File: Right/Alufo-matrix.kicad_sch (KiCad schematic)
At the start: 54 parts, among them K11 PG1350, K12 PG1350, K13 PG1350, K14 PG1350, K15 PG1350, K16 PG1350, K21 PG1350, K22 PG1350, K23 PG1350, K24 PG1350, K25 PG1350, K26 PG1350, K31 PG1350, K32 PG1350, K33 PG1350, K34 PG1350, K35 PG1350, K36 PG1350_1½U, K41 PG1350_1½U, K42 PG1350/SKQUCAA010

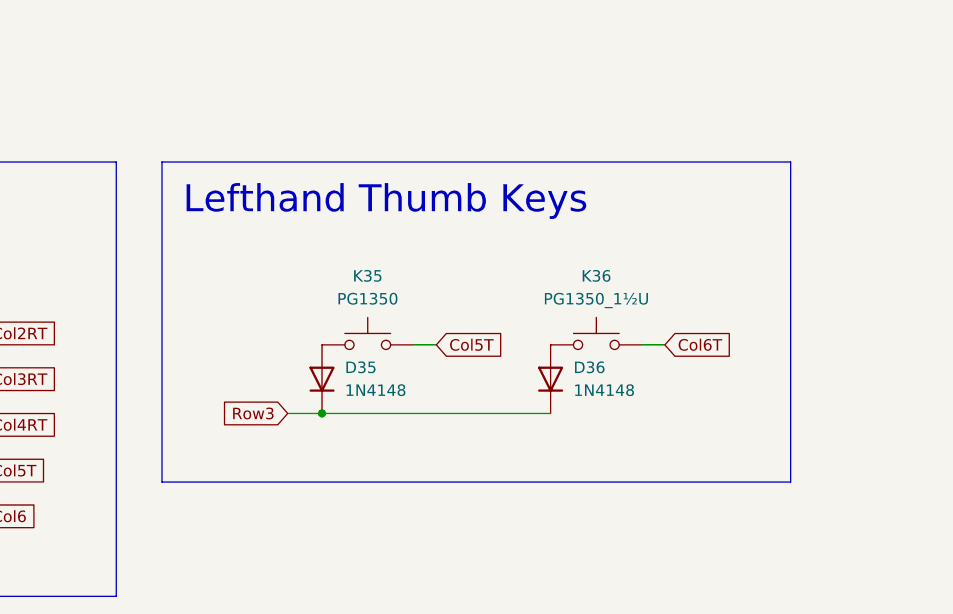
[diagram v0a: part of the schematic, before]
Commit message: Remove lefthand components from righthand board
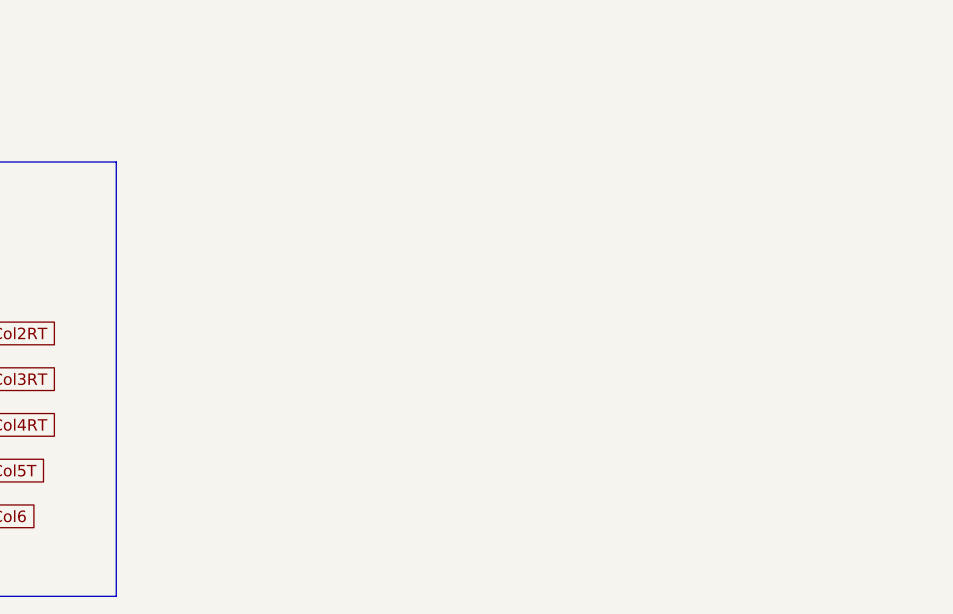
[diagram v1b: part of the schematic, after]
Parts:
- removed D35, D36: 1N4148, Project Library:D_SOD-123_Mod, symbol Device:D
- removed K35: PG1350, Project Library:SW_choc_v1_HS_CPG135001S30_1layer_1u, symbol Switch:SW_Push
- removed K36: PG1350_1½U, Project Library:SW_choc_v1_HS_CPG135001S30_1layer_1.5u, symbol Switch:SW_Push

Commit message: Realign columns on righthand side
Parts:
- renumbered D31 to D32, D32 to D33, D33 to D34, D34 to D35, K31 to K32, K32 to K33, K33 to K34, K34 to K35
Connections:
- net Col1T: no longer K32.1
- net Col5T: now also K35.1
- net Col2RT renamed Col2T
- net Col2T: now also K32.1; no longer K33.1
- net Col3RT renamed Col3T
- net Col3T: now also K33.1; no longer K34.1
- net Col4RT renamed Col4T
- net Col4T: now also K34.1; no longer K35.1

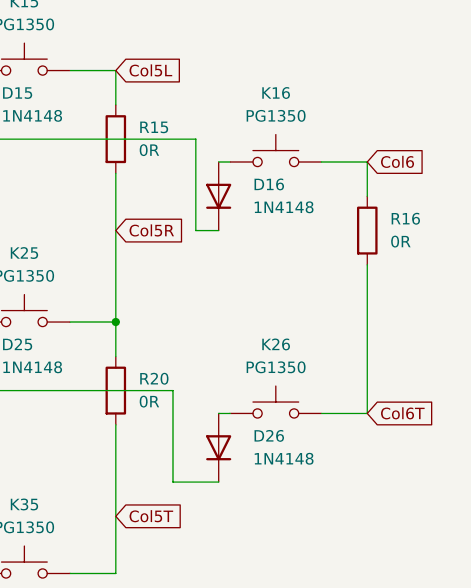
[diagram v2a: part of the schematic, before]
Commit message: Remove unneeded R16 from righthand side
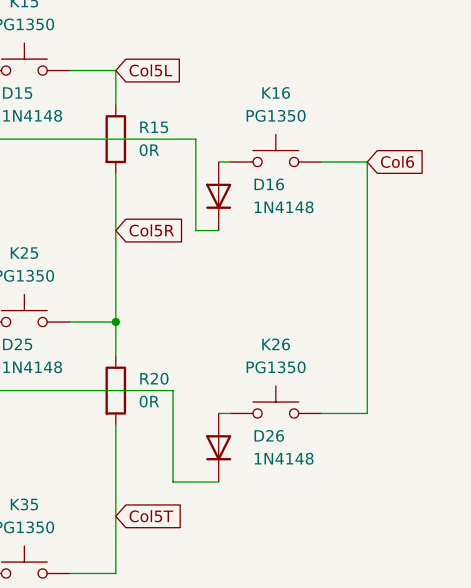
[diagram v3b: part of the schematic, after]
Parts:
- removed R16: 0R, Project Library:R_2010_5025Metric_Mod, symbol Device:R
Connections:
- net Col6T is gone; now on net Col6: K26.1
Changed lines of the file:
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@@
-	(wire
-		(pts
-			(xy 227.33 64.77) (xy 227.33 81.28)
-		)
-		(stroke
-			(width 0)
-			(type default)
-		)
-	)
 	(wire
 		(pts
@@
 	(wire
 		(pts
-			(xy 227.33 53.34) (xy 227.33 57.15)
+			(xy 227.33 53.34) (xy 227.33 81.28)
 		)
 		(stroke
@@
 		(property "Intersheetrefs" "${INTERSHEET_REFS}"
 			(at 95.8765 73.66 0)
-			(effects
-				(font
-					(size 1.27 1.27)
-				)
-				(justify left)
-				(hide yes)
-			)
-		)
-	)
-	(global_label "Col6T"
-		(shape input)
-		(at 227.33 81.28 0)
-		(fields_autoplaced yes)
-		(effects
-			(font
-				(size 1.27 1.27)
-			)
-			(justify left)
-		)
-		(property "Intersheetrefs" "${INTERSHEET_REFS}"
-			(at 235.5765 81.28 0)
 			(effects
 				(font
@@
 					(unit 1)
 				)
-			)
-		)
-	)
-	(symbol
-		(lib_id "Device:R")
-		(at 227.33 60.96 0)
-		(unit 1)
-		(exclude_from_sim no)
-		(in_bom yes)
-		(on_board yes)
-		(dnp no)
-		(fields_autoplaced yes)
-		(property "Reference" "R16"
-			(at 229.87 59.6899 0)
-			(effects
-				(font
-					(size 1.27 1.27)
-				)
-				(justify left)
-			)
-		)
-		(property "Value" "0R"
-			(at 229.87 62.2299 0)
-			(effects
-				(font
-					(size 1.27 1.27)
-				)
-				(justify left)
-			)
-		)
-		(property "Footprint" "Project Library:R_2010_5025Metric_Mod"
-			(at 225.552 60.96 90)
-			(effects
-				(font
-					(size 1.27 1.27)
-				)
-				(hide yes)
-			)
-		)
-		(property "Datasheet" "~"
-			(at 227.33 60.96 0)
-			(effects
-				(font
-					(size 1.27 1.27)
-				)
-				(hide yes)
-			)
-		)
-		(property "Description" "Resistor"
-			(at 227.33 60.96 0)
-			(effects
-				(font
-					(size 1.27 1.27)
-				)
-				(hide yes)
-			)
-		)
-		(pin "1"
-		)
-		(pin "2"
-		)
-		(instances
-			(project "Alufo"
-				(path "/52f043ac-ccff-4c85-bc10-2db9d3c9e3f3/ba0213d9-9934-4194-9bec-bf394cd27126"
-					(reference "R16")
-					(unit 1)
-				)

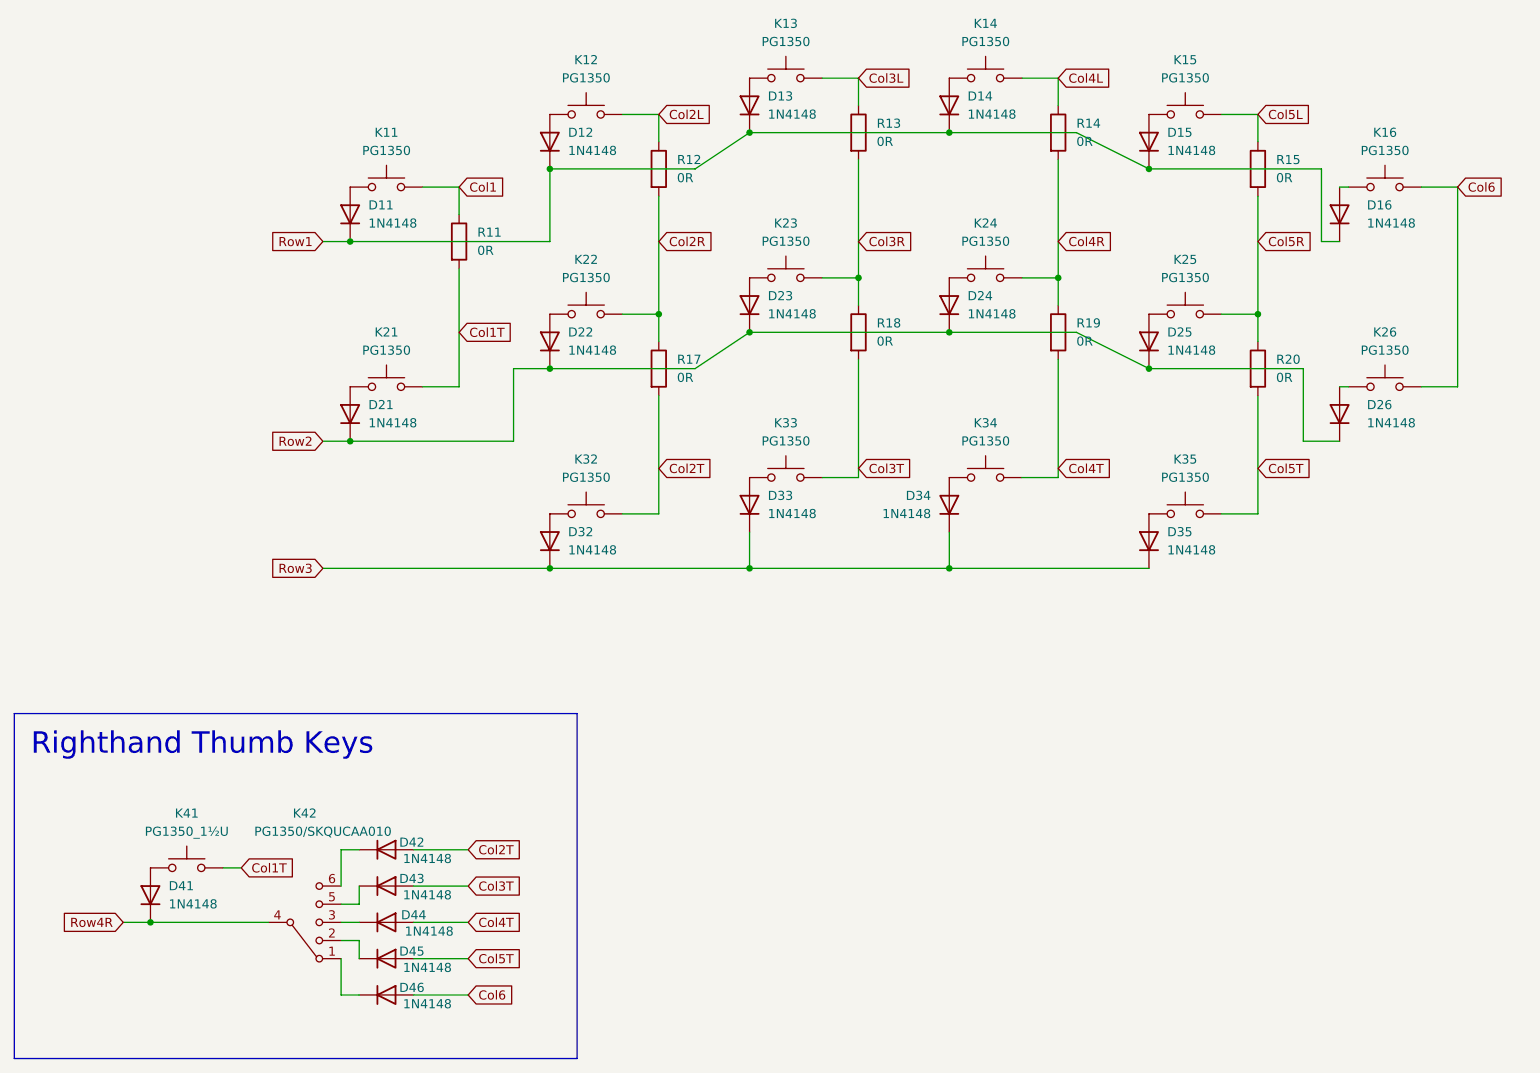
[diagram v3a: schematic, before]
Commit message: Route Row 2 under upper 0Ω resistors
TODO: Reconnect Column 6 to thumb row
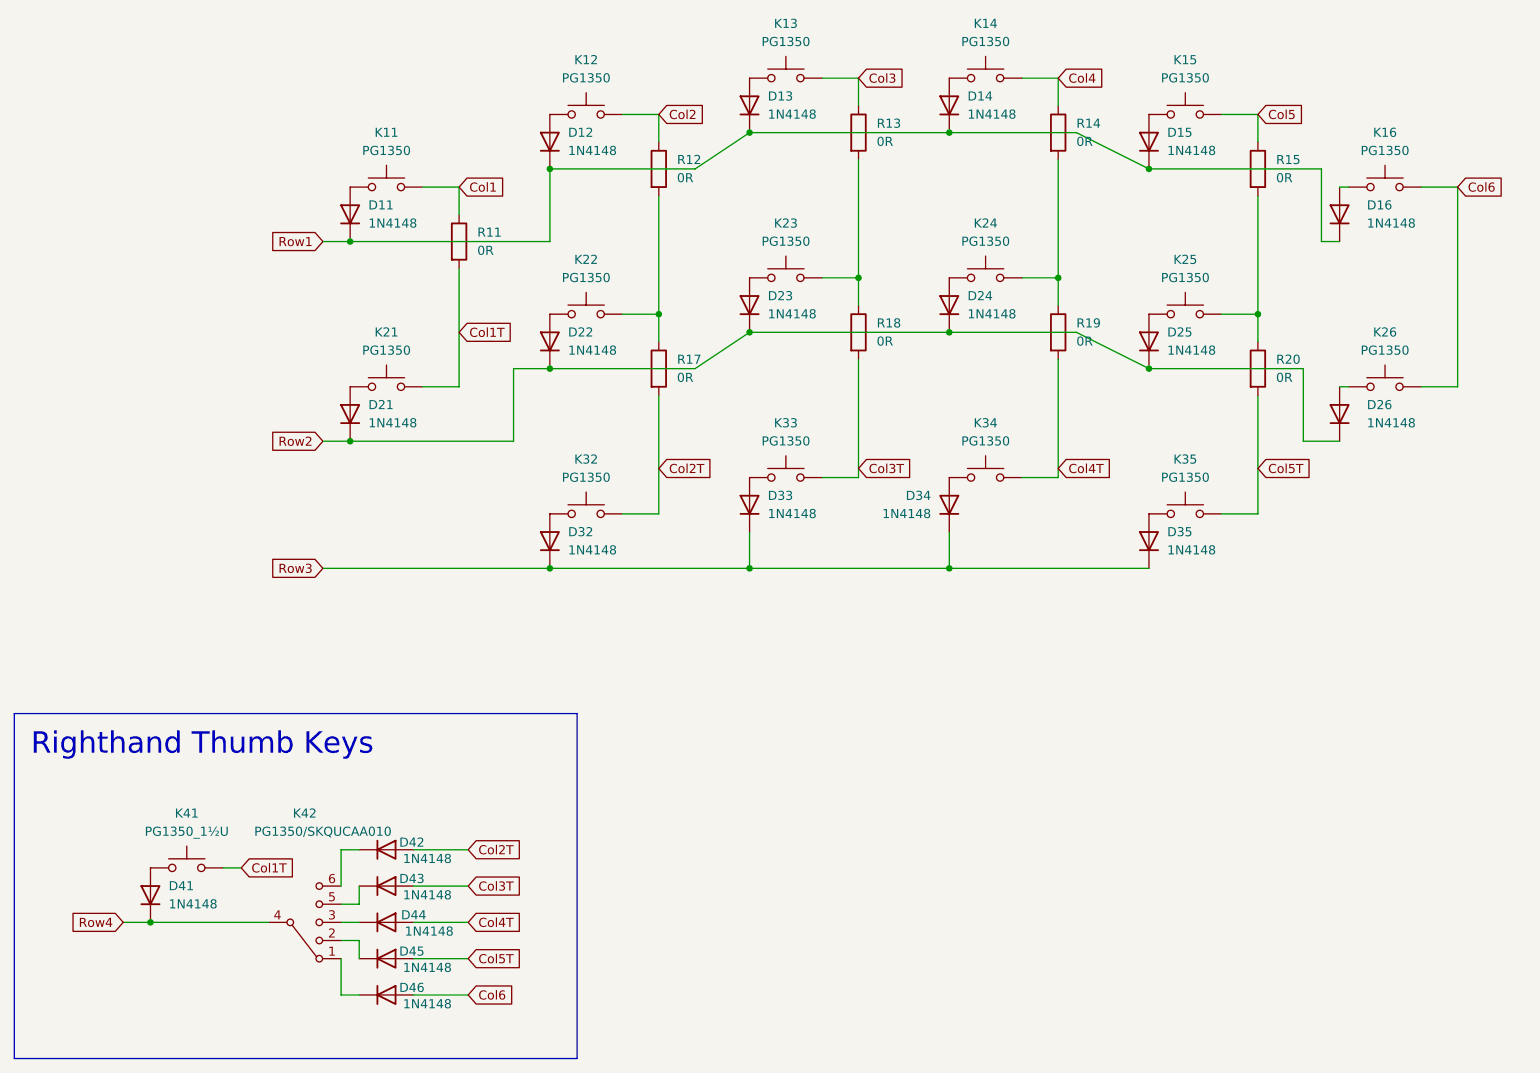
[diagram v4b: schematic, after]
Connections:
- net Col2L renamed Col2
- net Col2R: no longer names the net of K22.1, R12.2, R17.1
- net Col3L renamed Col3
- net Col3R: no longer names the net of K23.1, R13.2, R18.1
- net Col4L renamed Col4
- net Col4R: no longer names the net of K24.1, R14.2, R19.1
- net Col5L renamed Col5
- net Col5R: no longer names the net of K25.1, R15.2, R20.1
- net Row4R renamed Row4
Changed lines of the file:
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@@
-		)
-	)
-	(global_label "Col3R"
-		(shape input)
-		(at 143.51 60.96 0)
-		(fields_autoplaced yes)
-		(effects
-			(font
-				(size 1.27 1.27)
-			)
-			(justify left)
-		)
-		(property "Intersheetrefs" "${INTERSHEET_REFS}"
-			(at 152.0589 60.96 0)
-			(effects
-				(font
-					(size 1.27 1.27)
-				)
-				(justify left)
-				(hide yes)
-			)
 		)
 	)
@@
 		)
 	)
-	(global_label "Row4R"
+	(global_label "Row4"
 		(shape input)
 		(at 40.64 156.21 180)
@@
 		)
 		(property "Intersheetrefs" "${INTERSHEET_REFS}"
-			(at 31.4258 156.21 0)
+			(at 32.6958 156.21 0)
 			(effects
 				(font
@@
 		)
 	)
-	(global_label "Col5L"
+	(global_label "Col5"
 		(shape input)
 		(at 199.39 43.18 0)
@@
 		)
 		(property "Intersheetrefs" "${INTERSHEET_REFS}"
-			(at 207.697 43.18 0)
-			(effects
-				(font
-					(size 1.27 1.27)
-				)
-				(justify left)
-				(hide yes)
-			)
-		)
-	)
-	(global_label "Col4R"
-		(shape input)
-		(at 171.45 60.96 0)
-		(fields_autoplaced yes)
-		(effects
-			(font
-				(size 1.27 1.27)
-			)
-			(justify left)
-		)
-		(property "Intersheetrefs" "${INTERSHEET_REFS}"
-			(at 179.9989 60.96 0)
+			(at 206.6689 43.18 0)
 			(effects
 				(font
@@
 		)
 	)
-	(global_label "Col3L"
+	(global_label "Col3"
 		(shape input)
 		(at 143.51 38.1 0)
@@
 		)
 		(property "Intersheetrefs" "${INTERSHEET_REFS}"
-			(at 151.817 38.1 0)
-			(effects
-				(font
-					(size 1.27 1.27)
-				)
-				(justify left)
-				(hide yes)
-			)
-		)
-	)
-	(global_label "Col2R"
-		(shape input)
-		(at 115.57 60.96 0)
-		(fields_autoplaced yes)
-		(effects
-			(font
-				(size 1.27 1.27)
-			)
-			(justify left)
-		)
-		(property "Intersheetrefs" "${INTERSHEET_REFS}"
-			(at 124.1189 60.96 0)
+			(at 150.7889 38.1 0)
 			(effects
 				(font
@@
 		)
 	)
-	(global_label "Col4L"
+	(global_label "Col4"
 		(shape input)
 		(at 171.45 38.1 0)
@@
 		)
 		(property "Intersheetrefs" "${INTERSHEET_REFS}"
-			(at 179.757 38.1 0)
+			(at 178.7289 38.1 0)
 			(effects
 				(font
@@
 		)
 	)
-	(global_label "Col2L"
+	(global_label "Col2"
 		(shape input)
 		(at 115.57 43.18 0)
@@
 		)
 		(property "Intersheetrefs" "${INTERSHEET_REFS}"
-			(at 123.877 43.18 0)
+			(at 122.8489 43.18 0)
 			(effects
 				(font
@@
 			(effects
 				(font
-					(size 1.27 1.27)
-				)
-				(justify left)
-				(hide yes)
-			)
-		)
-	)
-	(global_label "Col5R"
-		(shape input)
-		(at 199.39 60.96 0)
-		(fields_autoplaced yes)
-		(effects
-			(font
-				(size 1.27 1.27)
-			)
-			(justify left)
-		)
-		(property "Intersheetrefs" "${INTERSHEET_REFS}"
-			(at 207.9389 60.96 0)
-			(effects
-				(font

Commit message: Route Row 3 under upper 0Ω resistors and remove lower 0Ω resistors
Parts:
- removed R17, R18, R19, R20: 0R, Project Library:R_2010_5025Metric_Mod, symbol Device:R
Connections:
- net Col2T: now also K22.1, R12.2
- net Col3T: now also K23.1, R13.2
- net Col4T: now also K24.1, R14.2
- net Col5T: now also K25.1, R15.2

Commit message: Manually add cutouts for 2010 resistors
Using middle-layer cutouts defined in the footprint no longer works as the resistors are now vertically aligned in relation to each rather than a set distance from the switch sockets.
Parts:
- R11, R12, R13, R14, R15: footprint Project Library:R_2010_5025Metric_Mod -> Resistor_SMD:R_2010_5025Metric
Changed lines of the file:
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@@
 			)
 		)
-		(property "Footprint" "Project Library:R_2010_5025Metric_Mod"
+		(property "Footprint" "Resistor_SMD:R_2010_5025Metric"
 			(at 141.732 45.72 90)
 			(effects
@@
 			)
 		)
-		(property "Footprint" "Project Library:R_2010_5025Metric_Mod"
+		(property "Footprint" "Resistor_SMD:R_2010_5025Metric"
 			(at 85.852 60.96 90)
 			(effects
@@
 			)
 		)
-		(property "Footprint" "Project Library:R_2010_5025Metric_Mod"
+		(property "Footprint" "Resistor_SMD:R_2010_5025Metric"
 			(at 113.792 50.8 90)
 			(effects
@@
 			)
 		)
-		(property "Footprint" "Project Library:R_2010_5025Metric_Mod"
+		(property "Footprint" "Resistor_SMD:R_2010_5025Metric"
 			(at 169.672 45.72 90)
 			(effects
@@
 			)
 		)
-		(property "Footprint" "Project Library:R_2010_5025Metric_Mod"
+		(property "Footprint" "Resistor_SMD:R_2010_5025Metric"
 			(at 197.612 50.8 90)
 			(effects
